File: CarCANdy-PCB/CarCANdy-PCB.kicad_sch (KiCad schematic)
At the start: 85 parts, among them J1 8P8C_Shielded, J10 ADC1, J11 ADC1, J12 ADC1, J13 Conn_01x02_Pin, J14 Conn_01x02_Pin, J15 Conn_01x02_Pin, J2 Power, J4 AUART1, J5 JSTVH3, J6 JSTVH3, J7 JSTVH3, J8 AUART1, K3 IM02, K4 IM02, K5 IM02, Q1 AO3400A, Q2 AO3400A, Q3 AO3400A, SW2 JS202011CQN, SW3 JS202011CQN, SW4 JS202011CQN, U1 LTV-357T, U2 ESP32-C3_SUPERMINI_TH, U3 SN65HVD233DR, U4 SN65HVD233DR, U5 SN65HVD233DR, U6 Teensy4.1, U7 LTV-357T, U8 LTV-357T

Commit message: added aux ports header to teensy
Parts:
- added H1, H2: MountingHole, MountingHole:MountingHole_3.2mm_M3, symbol Mechanical:MountingHole
- C2, C3, C4, C5, C6: footprint Capacitor_SMD:C_0603_1608Metric_Pad1.08x0.95mm_HandSolder -> Capacitor_SMD:C_1206_3216Metric_Pad1.33x1.80mm_HandSolder
- R1, R13, R14, R15, R16, R19, R2, R20, R21, R22, R23, R24, R25, R26, R27, R28, R3, R4, R5, R6, R7, R8: footprint Resistor_SMD:R_0603_1608Metric_Pad0.98x0.95mm_HandSolder -> Resistor_SMD:R_1206_3216Metric_Pad1.30x1.75mm_HandSolder
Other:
- note added: "high speed: JP 2->1 and solder RS slope control: JP 2->1 and open RS low power mode: JP 2->3"
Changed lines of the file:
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@@
 		)
 	)
+	(text "high speed: JP 2->1 and solder RS\nslope control: JP 2->1 and open RS\nlow power mode: JP 2->3"
+		(exclude_from_sim no)
+		(at 538.734 42.418 0)
+		(effects
+			(font
+				(size 1.27 1.27)
+			)
+		)
+	)
+	(text "high speed: JP 2->1 and solder RS\nslope control: JP 2->1 and open RS\nlow power mode: JP 2->3"
+		(exclude_from_sim no)
+		(at 745.49 41.402 0)
+		(effects
+			(font
+				(size 1.27 1.27)
+			)
+		)
+	)
 	(text "CAN2"
 		(exclude_from_sim no)
@@
 		)
 	)
+	(text "high speed: JP 2->1 and solder RS\nslope control: JP 2->1 and open RS\nlow power mode: JP 2->3"
+		(exclude_from_sim no)
+		(at 643.382 39.624 0)
+		(effects
+			(font
+				(size 1.27 1.27)
+			)
+		)
+	)
 	(text "5V ADC"
 		(exclude_from_sim no)
@@
 			)
 		)
-		(property "Footprint" "Resistor_SMD:R_0603_1608Metric_Pad0.98x0.95mm_HandSolder"
+		(property "Footprint" "Resistor_SMD:R_1206_3216Metric_Pad1.30x1.75mm_HandSolder"
 			(at 589.026 85.344 90)
 			(hide yes)
@@
 			)
 		)
-		(property "Footprint" "Resistor_SMD:R_0603_1608Metric_Pad0.98x0.95mm_HandSolder"
+		(property "Footprint" "Resistor_SMD:R_1206_3216Metric_Pad1.30x1.75mm_HandSolder"
 			(at 597.916 48.514 90)
 			(hide yes)
@@
 			)
 		)
-		(property "Footprint" "Resistor_SMD:R_0603_1608Metric_Pad0.98x0.95mm_HandSolder"
+		(property "Footprint" "Resistor_SMD:R_1206_3216Metric_Pad1.30x1.75mm_HandSolder"
 			(at 700.786 48.514 90)
 			(hide yes)
@@
 			)
 		)
-		(property "Footprint" "Resistor_SMD:R_0603_1608Metric_Pad0.98x0.95mm_HandSolder"
+		(property "Footprint" "Resistor_SMD:R_1206_3216Metric_Pad1.30x1.75mm_HandSolder"
 			(at 495.046 48.514 90)
 			(hide yes)
@@
 			)
 		)
-		(property "Footprint" "Resistor_SMD:R_0603_1608Metric_Pad0.98x0.95mm_HandSolder"
+		(property "Footprint" "Resistor_SMD:R_1206_3216Metric_Pad1.30x1.75mm_HandSolder"
 			(at 56.896 202.184 90)
 			(hide yes)
@@
 			)
 		)
-		(property "Footprint" "Resistor_SMD:R_0603_1608Metric_Pad0.98x0.95mm_HandSolder"
+		(property "Footprint" "Resistor_SMD:R_1206_3216Metric_Pad1.30x1.75mm_HandSolder"
 			(at 130.556 212.344 90)
 			(hide yes)
@@
 	)
 	(symbol
+		(lib_id "Mechanical:MountingHole")
+		(at 87.63 303.53 0)
+		(unit 1)
+		(body_style 1)
+		(exclude_from_sim no)
+		(in_bom no)
+		(on_board yes)
+		(in_pos_files yes)
+		(dnp no)
+		(fields_autoplaced yes)
+		(property "Reference" "H1"
+			(at 90.17 302.2599 0)
+			(show_name no)
+			(do_not_autoplace no)
+			(effects
+				(font
+					(size 1.27 1.27)
+				)
+				(justify left)
+			)
+		)
+		(property "Value" "MountingHole"
+			(at 90.17 304.7999 0)
+			(show_name no)
+			(do_not_autoplace no)
+			(effects
+				(font
+					(size 1.27 1.27)
+				)
+				(justify left)
+			)
+		)
+		(property "Footprint" "MountingHole:MountingHole_3.2mm_M3"
+			(at 87.63 303.53 0)
+			(hide yes)
+			(show_name no)
+			(do_not_autoplace no)
+			(effects
+				(font
+					(size 1.27 1.27)
+				)
+			)
+		)
+		(property "Datasheet" ""
+			(at 87.63 303.53 0)
+			(hide yes)
+			(show_name no)
+			(do_not_autoplace no)
+			(effects
+				(font
+					(size 1.27 1.27)
+				)
+			)
+		)
+		(property "Description" "Mounting Hole without connection"
+			(at 87.63 303.53 0)
+			(hide yes)
+			(show_name no)
+			(do_not_autoplace no)
+			(effects
+				(font
+					(size 1.27 1.27)
+				)
+			)
+		)
+		(instances
+			(project "CarCANdy-PCB"
+				(path "/971987f6-db6c-4f58-a887-69a69687dd52"
+					(reference "H1")
+					(unit 1)
+				)
+			)
+		)
+	)
+	(symbol
 		(lib_id "Jumper:SolderJumper_2_Open")
 		(at 485.14 73.66 90)
@@
 			)
 		)
-		(property "Footprint" "Resistor_SMD:R_0603_1608Metric_Pad0.98x0.95mm_HandSolder"
+		(property "Footprint" "Resistor_SMD:R_1206_3216Metric_Pad1.30x1.75mm_HandSolder"
 			(at 274.066 70.866 90)
 			(hide yes)
@@
 			)
 		)
-		(property "Footprint" "Resistor_SMD:R_0603_1608Metric_Pad0.98x0.95mm_HandSolder"
+		(property "Footprint" "Resistor_SMD:R_1206_3216Metric_Pad1.30x1.75mm_HandSolder"
 			(at 167.894 125.984 90)
 			(hide yes)
@@
 			)
 		)
-		(property "Footprint" "Resistor_SMD:R_0603_1608Metric_Pad0.98x0.95mm_HandSolder"
+		(property "Footprint" "Resistor_SMD:R_1206_3216Metric_Pad1.30x1.75mm_HandSolder"
 			(at 82.296 75.184 90)
 			(hide yes)
@@
 			)
 		)
-		(property "Footprint" "Capacitor_SMD:C_0603_1608Metric_Pad1.08x0.95mm_HandSolder"
+		(property "Footprint" "Capacitor_SMD:C_1206_3216Metric_Pad1.33x1.80mm_HandSolder"
 			(at 277.8252 59.69 0)
 			(hide yes)
@@
 			)
 		)
-		(property "Footprint" "Resistor_SMD:R_0603_1608Metric_Pad0.98x0.95mm_HandSolder"
+		(property "Footprint" "Resistor_SMD:R_1206_3216Metric_Pad1.30x1.75mm_HandSolder"
 			(at 291.084 128.016 90)
 			(hide yes)
@@
 			)
 		)
-		(property "Footprint" "Capacitor_SMD:C_0603_1608Metric_Pad1.08x0.95mm_HandSolder"
+		(property "Footprint" "Capacitor_SMD:C_1206_3216Metric_Pad1.33x1.80mm_HandSolder"
 			(at 80.9752 59.69 0)
 			(hide yes)
@@
 			)
 		)
-		(property "Footprint" "Resistor_SMD:R_0603_1608Metric_Pad0.98x0.95mm_HandSolder"
+		(property "Footprint" "Resistor_SMD:R_1206_3216Metric_Pad1.30x1.75mm_HandSolder"
 			(at 279.146 75.184 90)
 			(hide yes)
@@
 	)
 	(symbol
+		(lib_id "Mechanical:MountingHole")
+		(at 87.63 309.88 0)
+		(unit 1)
+		(body_style 1)
+		(exclude_from_sim no)
+		(in_bom no)
+		(on_board yes)
+		(in_pos_files yes)
+		(dnp no)
+		(fields_autoplaced yes)
+		(property "Reference" "H2"
+			(at 90.17 308.6099 0)
+			(show_name no)
+			(do_not_autoplace no)
+			(effects
+				(font
+					(size 1.27 1.27)
+				)
+				(justify left)
+			)
+		)
+		(property "Value" "MountingHole"
+			(at 90.17 311.1499 0)
+			(show_name no)
+			(do_not_autoplace no)
+			(effects
+				(font
+					(size 1.27 1.27)
+				)
+				(justify left)
+			)
+		)
+		(property "Footprint" "MountingHole:MountingHole_3.2mm_M3"
+			(at 87.63 309.88 0)
+			(hide yes)
+			(show_name no)
+			(do_not_autoplace no)
+			(effects
+				(font
+					(size 1.27 1.27)
+				)
+			)
+		)
+		(property "Datasheet" ""
+			(at 87.63 309.88 0)
+			(hide yes)
+			(show_name no)
+			(do_not_autoplace no)
+			(effects
+				(font
+					(size 1.27 1.27)
+				)
+			)
+		)
+		(property "Description" "Mounting Hole without connection"
+			(at 87.63 309.88 0)
+			(hide yes)
+			(show_name no)
+			(do_not_autoplace no)
+			(effects
+				(font
+					(size 1.27 1.27)
+				)
+			)
+		)
+		(instances
+			(project "CarCANdy-PCB"
+				(path "/971987f6-db6c-4f58-a887-69a69687dd52"
+					(reference "H2")
+					(unit 1)
+				)
+			)
+		)
+	)
+	(symbol
 		(lib_id "Diode:1N4148W")
 		(at 284.48 55.88 270)
@@
 			)
 		)
-		(property "Footprint" "Resistor_SMD:R_0603_1608Metric_Pad0.98x0.95mm_HandSolder"
+		(property "Footprint" "Resistor_SMD:R_1206_3216Metric_Pad1.30x1.75mm_HandSolder"
 			(at 77.216 70.866 90)
 			(hide yes)
@@
 			)
 		)
-		(property "Footprint" "Resistor_SMD:R_0603_1608Metric_Pad0.98x0.95mm_HandSolder"
+		(property "Footprint" "Resistor_SMD:R_1206_3216Metric_Pad1.30x1.75mm_HandSolder"
 			(at 194.564 128.016 90)
 			(hide yes)
@@
 			)
 		)
-		(property "Footprint" "Capacitor_SMD:C_0603_1608Metric_Pad1.08x0.95mm_HandSolder"
+		(property "Footprint" "Capacitor_SMD:C_1206_3216Metric_Pad1.33x1.80mm_HandSolder"
 			(at 181.3052 59.69 0)
 			(hide yes)
@@
 			)
 		)
-		(property "Footprint" "Capacitor_SMD:C_0603_1608Metric_Pad1.08x0.95mm_HandSolder"
+		(property "Footprint" "Capacitor_SMD:C_1206_3216Metric_Pad1.33x1.80mm_HandSolder"
 			(at 50.4952 215.9 0)
 			(hide yes)
@@
 			)
 		)
-		(property "Footprint" "Resistor_SMD:R_0603_1608Metric_Pad0.98x0.95mm_HandSolder"
+		(property "Footprint" "Resistor_SMD:R_1206_3216Metric_Pad1.30x1.75mm_HandSolder"
 			(at 130.556 202.184 90)
 			(hide yes)
@@
 			)
 		)
-		(property "Footprint" "Capacitor_SMD:C_0603_1608Metric_Pad1.08x0.95mm_HandSolder"
+		(property "Footprint" "Capacitor_SMD:C_1206_3216Metric_Pad1.33x1.80mm_HandSolder"
 			(at 124.1552 215.9 0)
 			(hide yes)
@@
 			)
 		)
-		(property "Footprint" "Resistor_SMD:R_0603_1608Metric_Pad0.98x0.95mm_HandSolder"
+		(property "Footprint" "Resistor_SMD:R_1206_3216Metric_Pad1.30x1.75mm_HandSolder"
 			(at 182.626 75.184 90)
 			(hide yes)
@@
 			)
 		)
-		(property "Footprint" "Resistor_SMD:R_0603_1608Metric_Pad0.98x0.95mm_HandSolder"
+		(property "Footprint" "Resistor_SMD:R_1206_3216Metric_Pad1.30x1.75mm_HandSolder"
 			(at 264.414 125.984 90)
 			(hide yes)
@@
 			)
 		)
-		(property "Footprint" "Resistor_SMD:R_0603_1608Metric_Pad0.98x0.95mm_HandSolder"
+		(property "Footprint" "Resistor_SMD:R_1206_3216Metric_Pad1.30x1.75mm_HandSolder"
 			(at 94.234 128.016 90)
 			(hide yes)
@@
 			)
 		)
-		(property "Footprint" "Resistor_SMD:R_0603_1608Metric_Pad0.98x0.95mm_HandSolder"
+		(property "Footprint" "Resistor_SMD:R_1206_3216Metric_Pad1.30x1.75mm_HandSolder"
 			(at 486.156 85.344 90)
 			(hide yes)
@@
 			)
 		)
-		(property "Footprint" "Resistor_SMD:R_0603_1608Metric_Pad0.98x0.95mm_HandSolder"
+		(property "Footprint" "Resistor_SMD:R_1206_3216Metric_Pad1.30x1.75mm_HandSolder"
 			(at 67.564 125.984 90)
 			(hide yes)
@@
 			)
 		)
-		(property "Footprint" "Resistor_SMD:R_0603_1608Metric_Pad0.98x0.95mm_HandSolder"
+		(property "Footprint" "Resistor_SMD:R_1206_3216Metric_Pad1.30x1.75mm_HandSolder"
 			(at 177.546 70.866 90)
 			(hide yes)
@@
 			)
 		)
-		(property "Footprint" "Resistor_SMD:R_0603_1608Metric_Pad0.98x0.95mm_HandSolder"
+		(property "Footprint" "Resistor_SMD:R_1206_3216Metric_Pad1.30x1.75mm_HandSolder"
 			(at 691.896 85.344 90)
 			(hide yes)
@@
 			)
 		)
-		(property "Footprint" "Resistor_SMD:R_0603_1608Metric_Pad0.98x0.95mm_HandSolder"
+		(property "Footprint" "Resistor_SMD:R_1206_3216Metric_Pad1.30x1.75mm_HandSolder"
 			(at 56.896 212.344 90)
 			(hide yes)

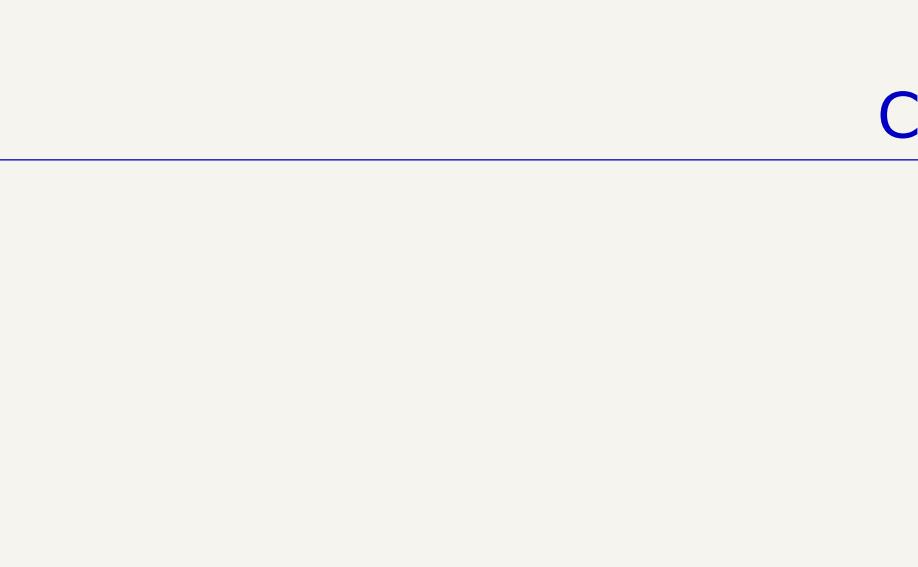
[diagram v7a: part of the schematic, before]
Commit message: simplified CANDB json
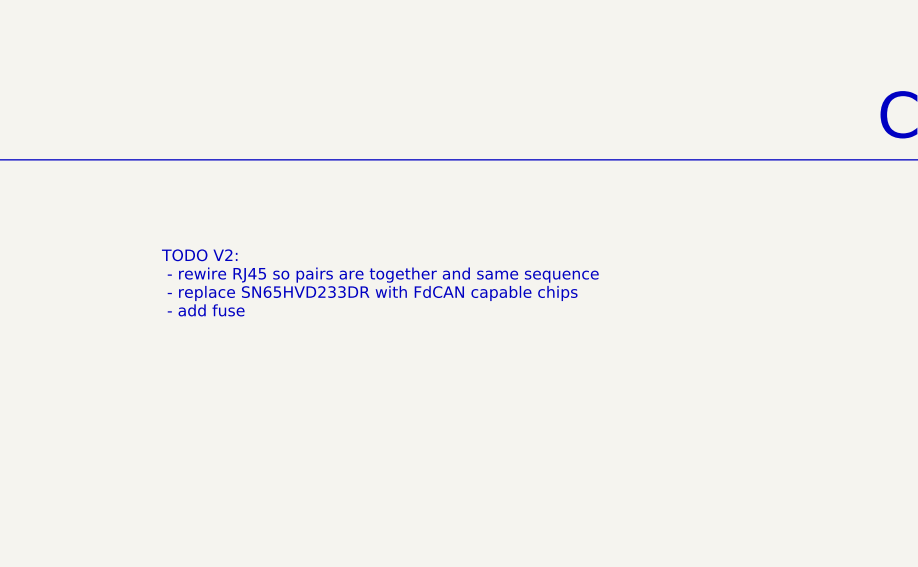
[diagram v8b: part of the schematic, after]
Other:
- note added: "TODO V2: - rewire RJ45 so pairs are together and same sequence - replace SN65HVD233DR with FdCAN capable chips - add fuse"
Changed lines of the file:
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@@
+		)
+	)
+	(text "TODO V2: \n - rewire RJ45 so pairs are together and same sequence\n - replace SN65HVD233DR with FdCAN capable chips\n - add fuse"
+		(exclude_from_sim no)
+		(at 547.37 163.83 0)
+		(effects
+			(font
+				(size 1.27 1.27)
+			)
+			(justify left)
 		)
 	)
